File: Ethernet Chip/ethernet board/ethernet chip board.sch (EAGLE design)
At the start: 33 parts

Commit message: Started Ethernet Board Layout
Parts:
- R20: value 10k -> 1.5k
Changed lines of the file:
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@@
 <?xml version="1.0" encoding="utf-8"?>
 <!DOCTYPE eagle SYSTEM "eagle.dtd">
-<eagle version="7.3.0">
+<eagle version="7.4.0">
 <drawing>
 <settings>
@@
 <part name="R15" library="resistor" deviceset="R-US_" device="R0603" value="27R"/>
 <part name="R19" library="resistor" deviceset="R-US_" device="R0603" value="27R"/>
-<part name="R20" library="resistor" deviceset="R-US_" device="R0603" value="10k"/>
+<part name="R20" library="resistor" deviceset="R-US_" device="R0603" value="1.5k"/>
 <part name="+3V2" library="supply1" deviceset="+3V3" device=""/>
 <part name="GND5" library="SparkFun-Aesthetics" deviceset="GND" device=""/>

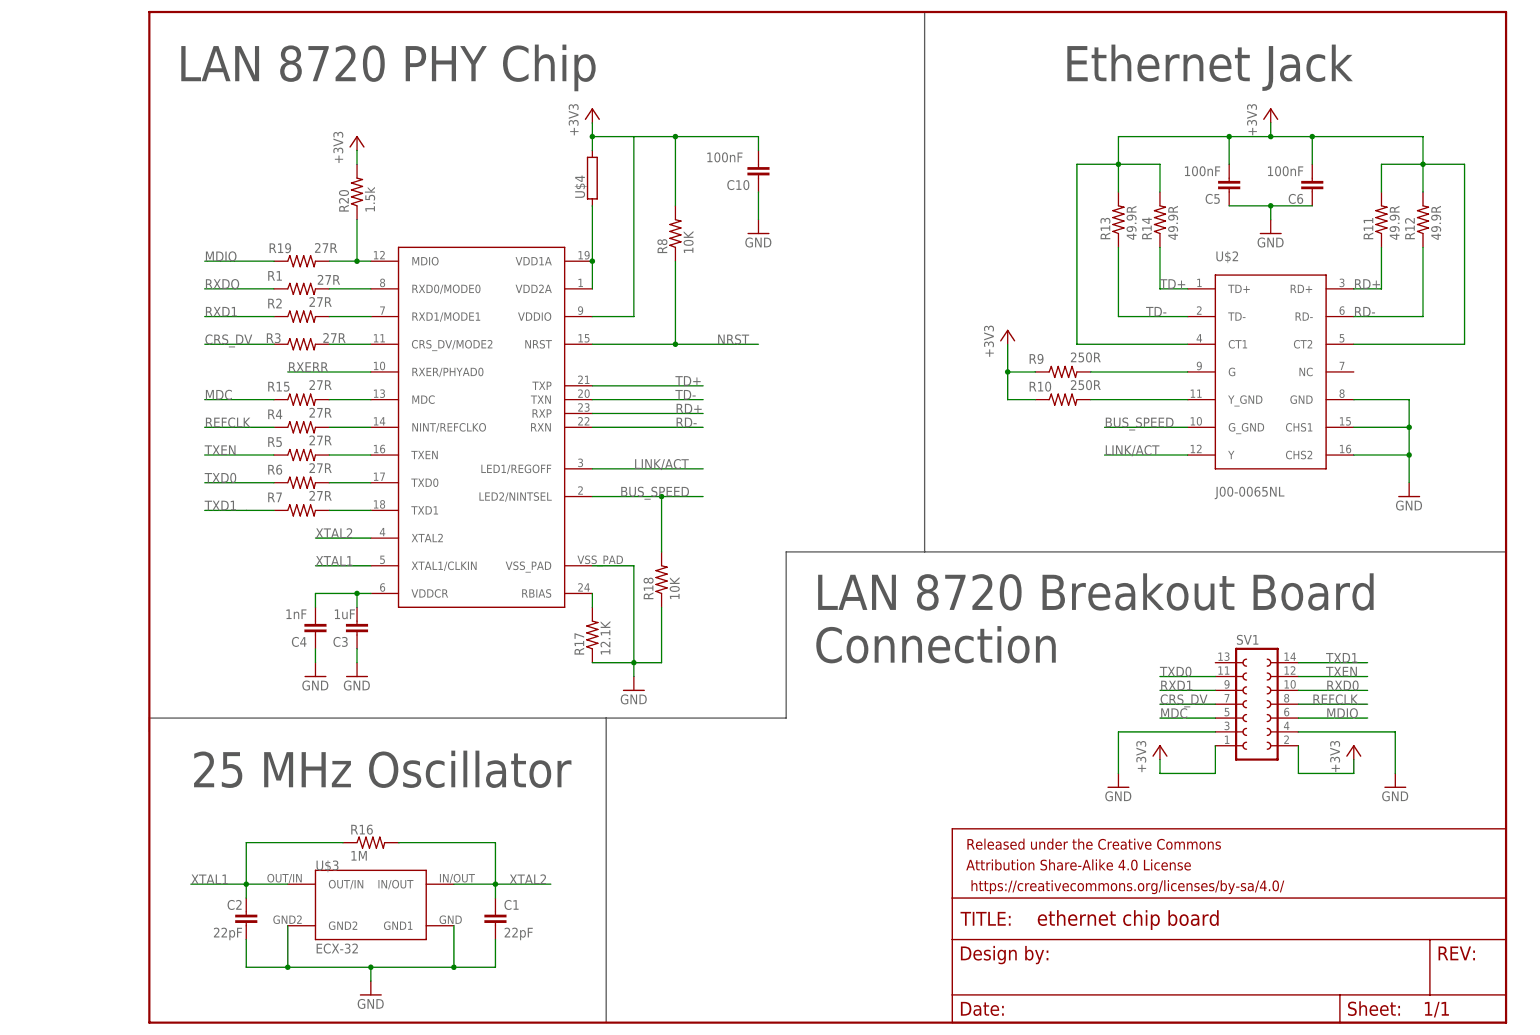
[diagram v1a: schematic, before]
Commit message: Worked on the board layout for the ethernet circuit
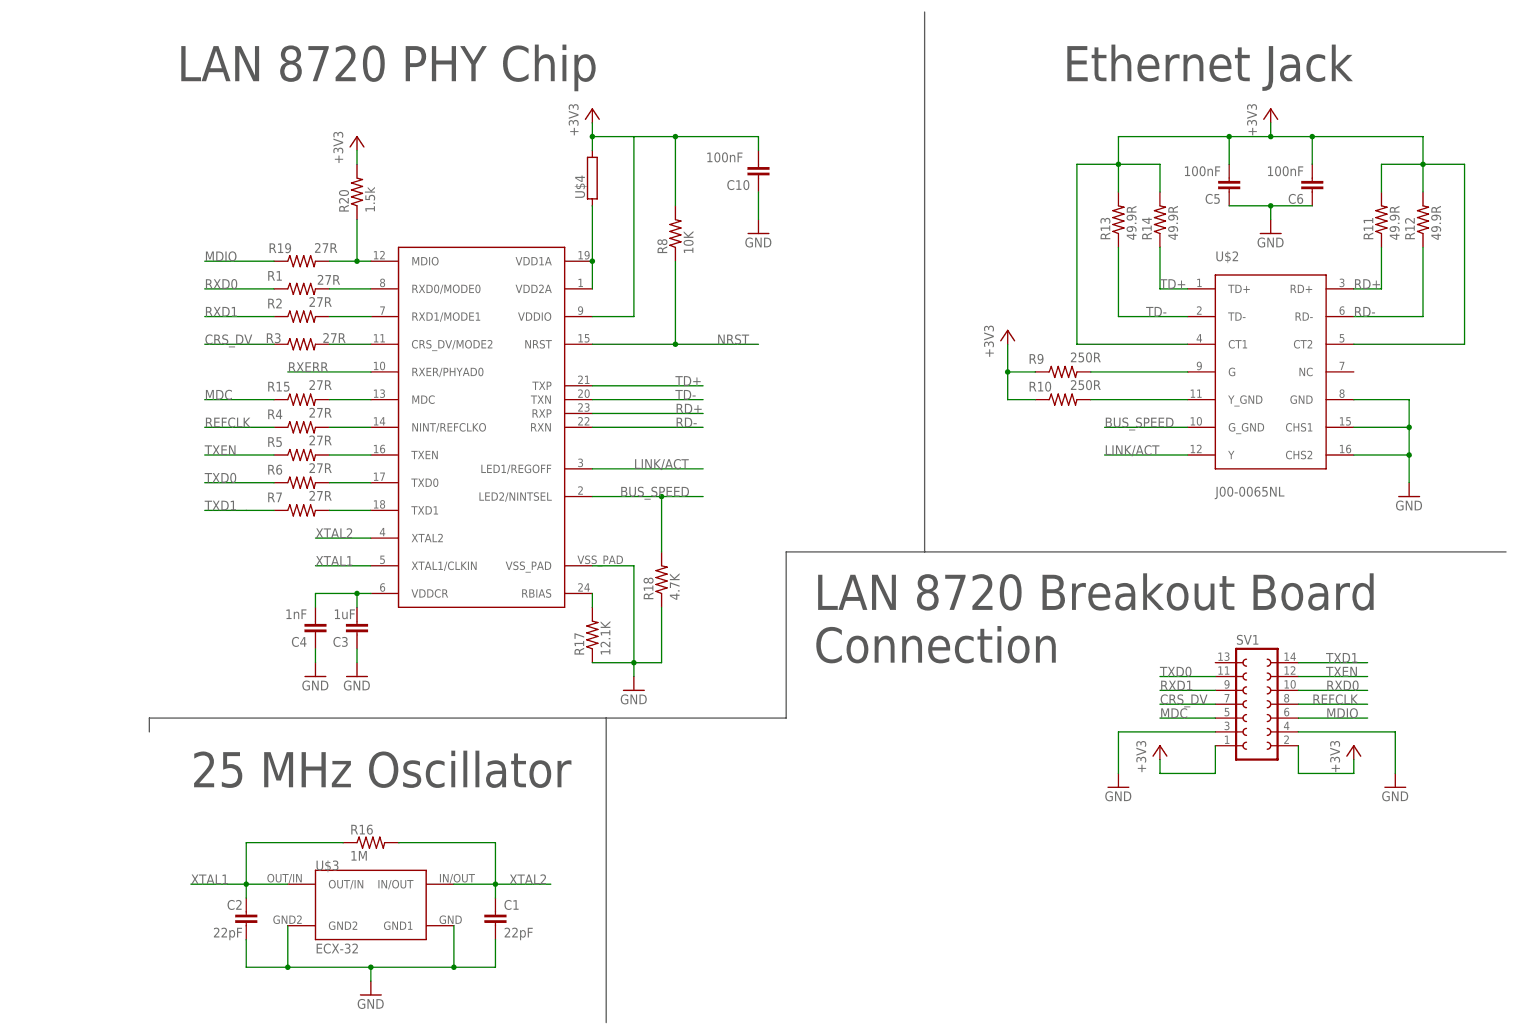
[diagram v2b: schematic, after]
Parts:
- removed FRAME1: FRAME-LETTER, SparkFun-Aesthetics:FRAME-LETTER
- R18: value 10K -> 4.7K
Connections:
- removed net RXDO: R1.1
- net RXD0: now also R1.1
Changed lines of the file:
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@@
 <?xml version="1.0" encoding="utf-8"?>
 <!DOCTYPE eagle SYSTEM "eagle.dtd">
-<eagle version="7.4.0">
+<eagle version="7.3.0">
 <drawing>
 <settings>
@@
 </classes>
 <parts>
-<part name="FRAME1" library="SparkFun-Aesthetics" deviceset="FRAME-LETTER" device=""/>
 <part name="C1" library="eagle-ltspice" deviceset="C" device="C0603" value="22pF"/>
 <part name="C2" library="eagle-ltspice" deviceset="C" device="C0603" value="22pF"/>
@@
 <part name="R16" library="resistor" deviceset="R-US_" device="R0603" value="1M"/>
 <part name="R17" library="resistor" deviceset="R-US_" device="R0603" value="12.1K"/>
-<part name="R18" library="resistor" deviceset="R-US_" device="R0603" value="10K"/>
+<part name="R18" library="resistor" deviceset="R-US_" device="R0603" value="4.7K"/>
 <part name="U$2" library="EthernetChip" deviceset="J00-0065NL" device=""/>
 <part name="U$3" library="Other" deviceset="ECX-32" device=""/>
@@
 <part name="C10" library="eagle-ltspice" deviceset="C" device="C0603" value="100nF"/>
 <part name="GND8" library="SparkFun-Aesthetics" deviceset="GND" device=""/>
+<part name="FRAME1" library="frames" deviceset="LETTER_L" device=""/>
 </parts>
 <sheets>
@@
 </plain>
 <instances>
-<instance part="FRAME1" gate="G$1" x="-127" y="-96.52"/>
-<instance part="FRAME1" gate="V" x="20.32" y="-96.52"/>
 <instance part="C1" gate="G$1" x="-63.5" y="-76.2"/>
 <instance part="C2" gate="G$1" x="-109.22" y="-76.2" smashed="yes">
@@
 </instance>
 <instance part="GND8" gate="1" x="-15.24" y="48.26"/>
+<instance part="FRAME1" gate="G$1" x="-127" y="-96.52"/>
+<instance part="FRAME1" gate="G$2" x="20.32" y="-96.52"/>
 </instances>
 <busses>
@@
 </segment>
 </net>
-<net name="RXDO" class="0">
-<segment>
-<wire x1="-104.14" y1="38.1" x2="-116.84" y2="38.1" width="0.1524" layer="91"/>
-<pinref part="R1" gate="G$1" pin="1"/>
-<label x="-116.84" y="38.1" size="1.778" layer="95"/>
-</segment>
-</net>
 <net name="TXEN" class="0">
 <segment>
@@
 <label x="88.9" y="-35.56" size="1.778" layer="95"/>
 </segment>
-</net>
+<segment>
+<wire x1="-104.14" y1="38.1" x2="-116.84" y2="38.1" width="0.1524" layer="91"/>
+<pinref part="R1" gate="G$1" pin="1"/>
+<label x="-116.84" y="38.1" size="1.778" layer="95"/>
+</segment>
+</net>

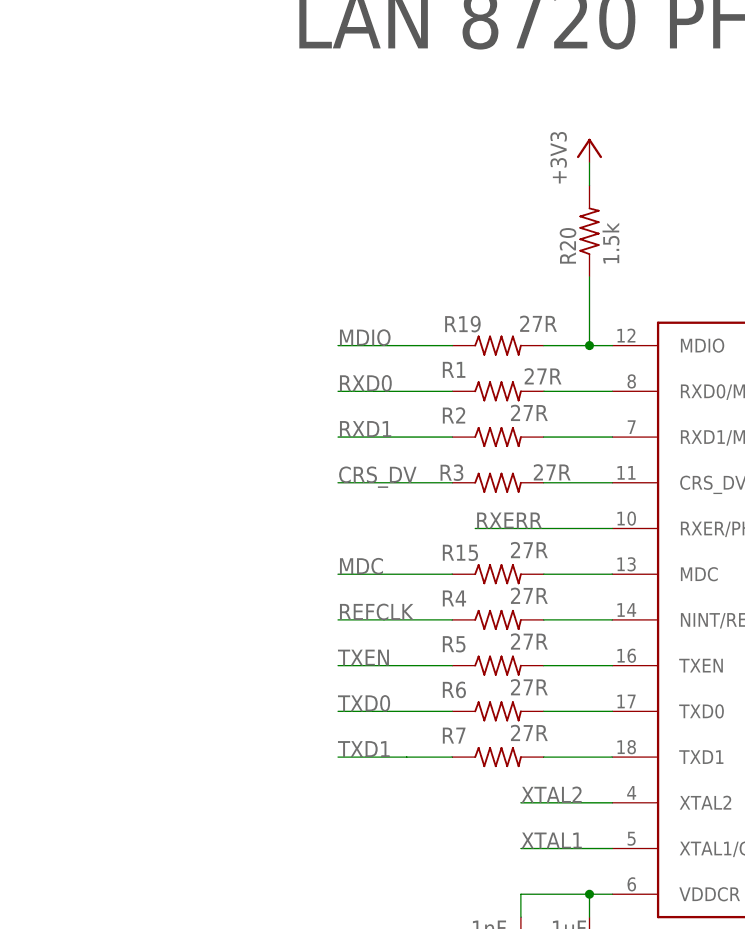
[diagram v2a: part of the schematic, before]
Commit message: updated the ethernet board
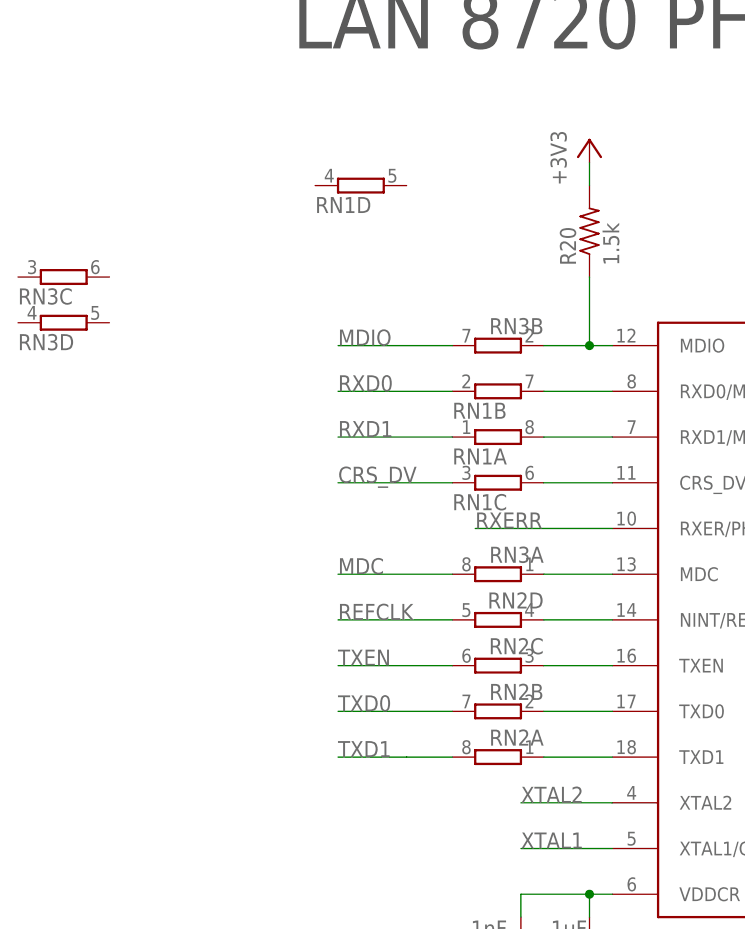
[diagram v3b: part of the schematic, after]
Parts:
- removed R1, R15, R19, R2, R3, R4, R5, R6, R7: 27R, resistor:R-US_R0603
- added RN1, RN2, RN3: (no value), resistor-dil:4R-NCAY16
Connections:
- net CRS_DV: now also RN1C.1; no longer R3.1
- net MDC: now also RN3A.2; no longer R15.1
- net MDE: now also RN3A.1; no longer R15.2
- net MDIO: now also RN3B.2; no longer R19.1
- net N$1: now also RN1B.2; no longer R1.2
- net N$10: now also RN2A.1; no longer R7.2
- net N$12: now also RN3B.1; no longer R19.2
- net N$2: now also RN1A.2; no longer R2.2
- net N$5: now also RN1C.2; no longer R3.2
- net N$7: now also RN2D.1; no longer R4.2
- net N$8: now also RN2C.1; no longer R5.2
- net N$9: now also RN2B.1; no longer R6.2
- net REFCLK: now also RN2D.2; no longer R4.1
- net RXD0: now also RN1B.1; no longer R1.1
- net RXD1: now also RN1A.1; no longer R2.1
- net TXD0: now also RN2B.2; no longer R6.1
- net TXD1: now also RN2A.2; no longer R7.1
- net TXEN: now also RN2C.2; no longer R5.1
